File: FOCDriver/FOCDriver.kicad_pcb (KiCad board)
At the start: 4 copper layers, 80 x 80 mm, 306 parts, among them J1 Conn_02x06_Odd_Even, J10 Conn_01x04, J11 Conn_01x04, J12 Screw_Terminal_01x02, J2 Conn_02x06_Odd_Even, J3 Conn_02x06_Odd_Even, J4 Conn_02x05_Odd_Even, J5 Screw_Terminal_01x02, J6 Conn_01x03_Pin, J7 Conn_01x03_Pin, J8 Conn_01x03_Pin, J9 Conn_01x04, M1 Fan_Tacho_PWM, Q1 NMOS, Q2 SIR422DP-T1-GE3, SW1 SW_Push, SW2 SW_Push, SW3 SW_Push, U1 STM32H725IGTx, U10 DRV8316CR, U11 MCP1501-25xSN, U12 TMP1075DSG, U13 LM22676MR-5, U14 Si4435DDY, U15 DRV8316CR, U16 DRV8316CR, U17 ZXCT1109, U2 LM324, U3 24LC64, U4 LM324, U5 AP7375-30SA-7, U6 AMS1117-3.3, U7 LM324, Y1 Crystal_GND24

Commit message: Update
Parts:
- added C90: 100n, Footprints:Nice_0603C, F.Cu at (52.5, 97.5)
- added D8: APT2012SYCK, LED_SMD:LED_0805_2012Metric, F.Cu at (65.9, 101.4)
- added D9: APT2012SYCK, LED_SMD:LED_0805_2012Metric, F.Cu at (65.9, 103.3)
- added R80: DNP, Footprints:Nice_0402DNP, F.Cu at (52.8, 98.8)
- added R81: 1k, Footprints:Nice_0402R, F.Cu at (63.0, 101.5)
- added R82: 1k, Footprints:Nice_0402R, F.Cu at (63.6, 103.2)
- added kibuzzard-67FE68DD: G***, kibuzzard-67FE68DD, B.Cu at (52.3, 101.2)
- added kibuzzard-67FE6936: G***, kibuzzard-67FE6936, B.Cu at (52.2, 90.0)
- added kibuzzard-67FE6963: G***, kibuzzard-67FE6963, B.Cu at (52.2, 78.8)
- C43: footprint Capacitor_SMD:CP_Elec_10x10 -> Capacitor_SMD:CP_Elec_8x10.5
- C68, C69, C83: footprint Capacitor_SMD:CP_Elec_10x10 -> Capacitor_SMD:CP_Elec_10x10.5
- C92, C95, C96, C97: footprint Footprints:Nice_0805C -> Footprints:Nice_0603C
- D1: value 10V zener -> BZX384-B10,115
- D3, D4, D5, D6, D7: value LED -> APT2012SYCK
- F1: value 30R300U / 30R500U -> 30R500U
- L1: value L_Ferrite -> BLM18AG471SN1D
- Q1: value NMOS -> 2N7002
- R51, R52, R65: value 470 -> 470R
- R62, R69, R70, R74, R75: value 100 -> 100R
- RN1: value R_Pack04 -> EXB-38V102JV
- RN2, RN3, RN4, RN5: value R_Pack04 -> EXB-N8N220JX
- U11: value MCP1501-25xSN -> MCP1501-25E/SN
- Y1: value Crystal_GND24 -> ECS-250-18-33-JGN-TR3
- moved R2 10.5 mm to (51.5, 121.6), turned to 180 degrees
- moved D1 7.83 mm to (52.2, 120.1)
- moved R64 2.24 mm to (52.2, 101.2), turned to -90 degrees
- moved TP59 1.73 mm to (80.7, 90.4)
- moved TP4 1.06 mm to (62.2, 103.5)
- moved C43 0.82 mm to (57.5, 80.9)
- moved C69 0.58 mm to (78.7, 83.5)
- moved C68 0.50 mm to (100.0, 83.5)
- moved C83 0.40 mm to (121.6, 83.5)
- moved C97 0.30 mm to (111.3, 64.9)
- moved TP56 0.22 mm to (73.0, 107.3)
- moved J10 0.20 mm to (127.8, 91.1)
- moved R76 0.20 mm to (126.2, 95.1)
- moved R77 0.20 mm to (126.2, 97.1)
- moved kibuzzard-67FA3F2F 0.20 mm to (124.0, 90.6)
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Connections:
- net LED1 renamed /MCU/LED1
- net LED2 renamed /MCU/LED2
- net LED3 renamed /MCU/LED3
- net LED4 renamed /MCU/LED4
- U1 pad 50: /MCU/TIM2_CH1 -> unconnected-(U1-PA5-Pad50)
- U13 pad 2: unconnected-(U13-NC-Pad2) -> Net-(U13-SS)
- U13 pad 3: unconnected-(U13-NC-Pad3) -> Net-(U13-RT)
- U14 pad 1: Net-(J5-Pin_1) -> Net-(D1-K)
- U14 pad 2: Net-(J5-Pin_1) -> Net-(D1-K)
- U14 pad 3: Net-(J5-Pin_1) -> Net-(D1-K)
- U14 pad 5: Net-(D1-K) -> Net-(J5-Pin_1)
- U14 pad 6: Net-(D1-K) -> Net-(J5-Pin_1)
- U14 pad 7: Net-(D1-K) -> Net-(J5-Pin_1)
- U14 pad 8: Net-(D1-K) -> Net-(J5-Pin_1)
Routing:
- net +5V: track 68.7 -> 94.6 mm, vias 16 -> 23
- net GND: track 228.2 -> 243.9 mm, vias 328 -> 383
- net Net-(D1-K): track 0.00 -> 4.66 mm
- net MTR2_SDA: track 76.3 -> 80.0 mm
- net Net-(U2D-+): track 10.5 -> 7.24 mm
- net MTRx_SLEEP: track 104.8 -> 107.5 mm
- net /Motor1/NTC: track 48.3 -> 46.1 mm
- net EN_CLAMP: track 51.3 -> 53.3 mm
- net Net-(U13-SS): track 0.00 -> 1.86 mm
- net MTR3_SOA: track 30.5 -> 32.3 mm
- net MTR2_SCL: track 79.6 -> 81.4 mm
- net Net-(U13-RT): track 0.00 -> 1.75 mm
- net Net-(D9-A): track 0.00 -> 1.53 mm
- net Net-(D1-A): track 2.80 -> 4.31 mm
- net I2C4_SDA: track 9.32 -> 10.8 mm
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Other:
- board text added: "+3V3"
- board text added: "1"
- board text added: "2"
- board text added: "3"
- board text added: "4"
- board text added: "Im"
- board text added: "Vm"
- board text removed: "Imon"
- board text removed: "Vmotor"

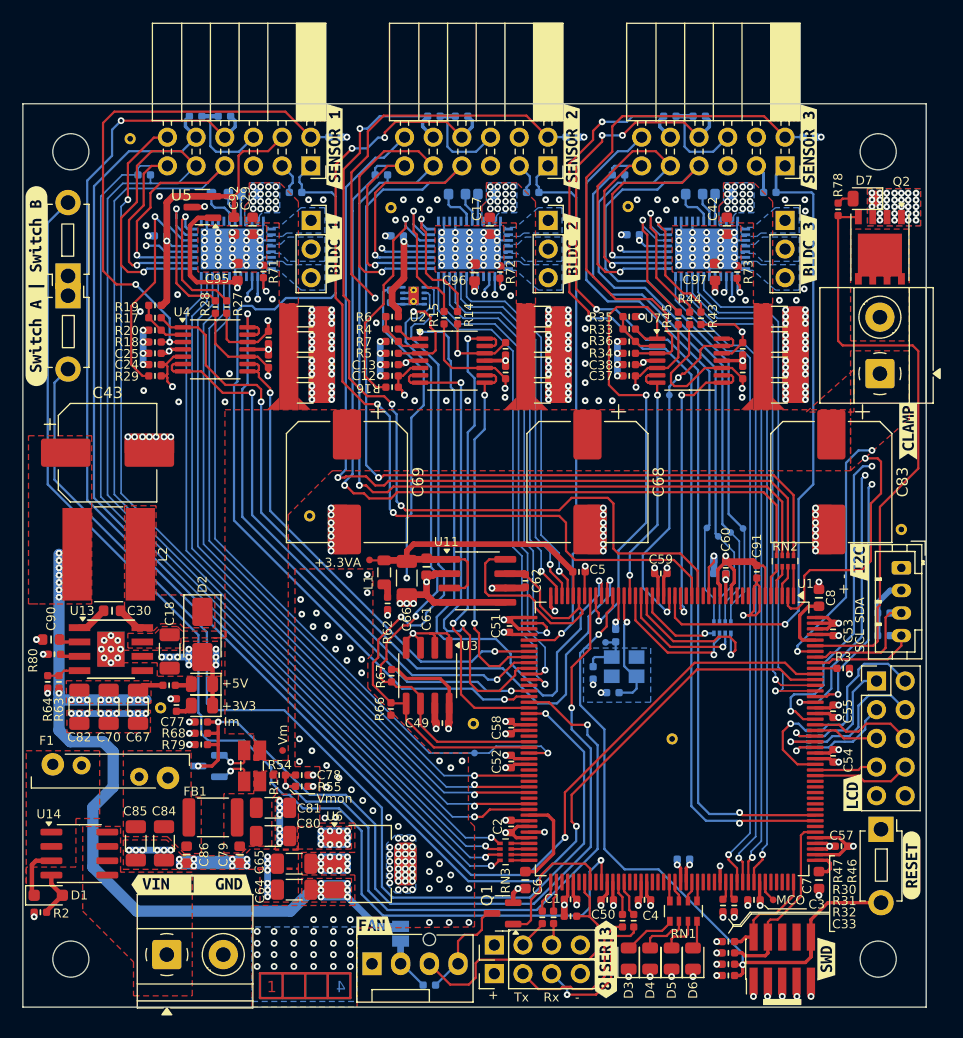
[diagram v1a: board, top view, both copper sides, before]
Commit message: Sensor PCB fixes labels
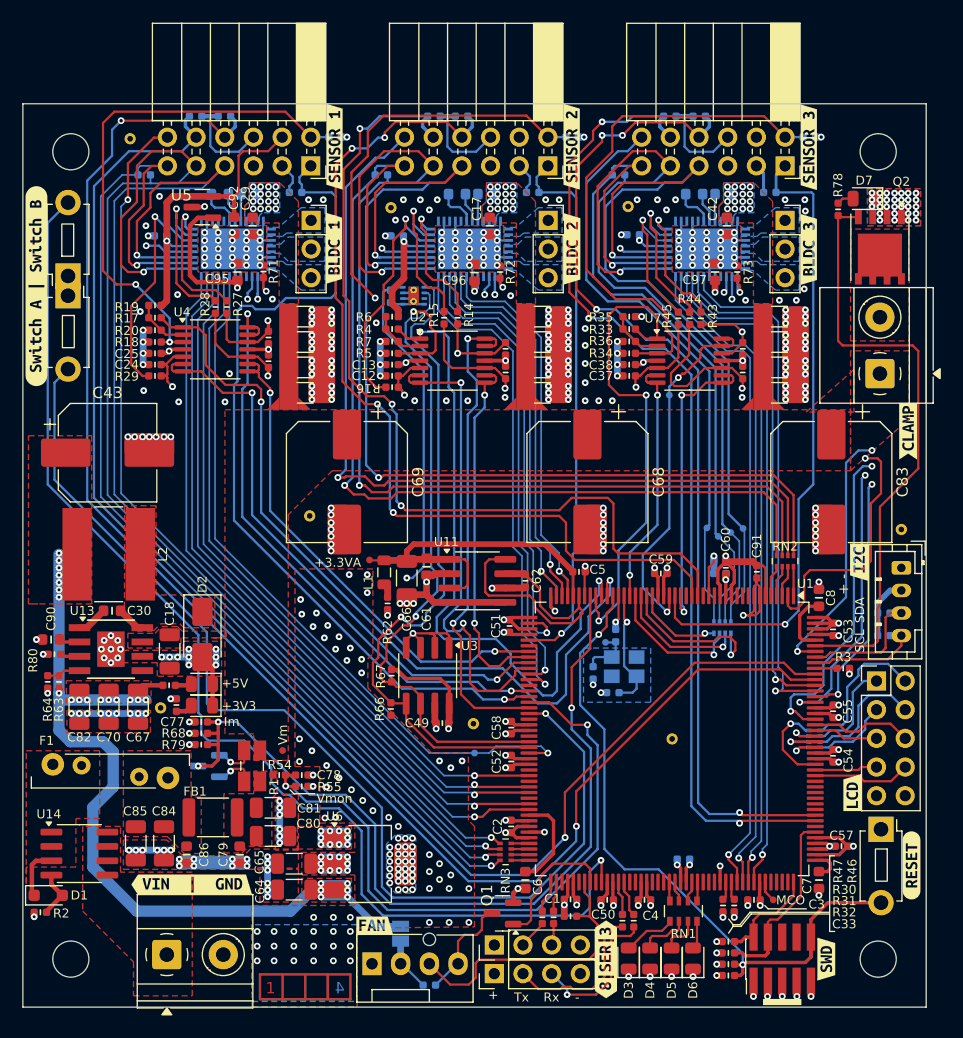
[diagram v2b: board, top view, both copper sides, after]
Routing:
- net VDD: track 127.6 -> 127.8 mm, vias 136 -> 130

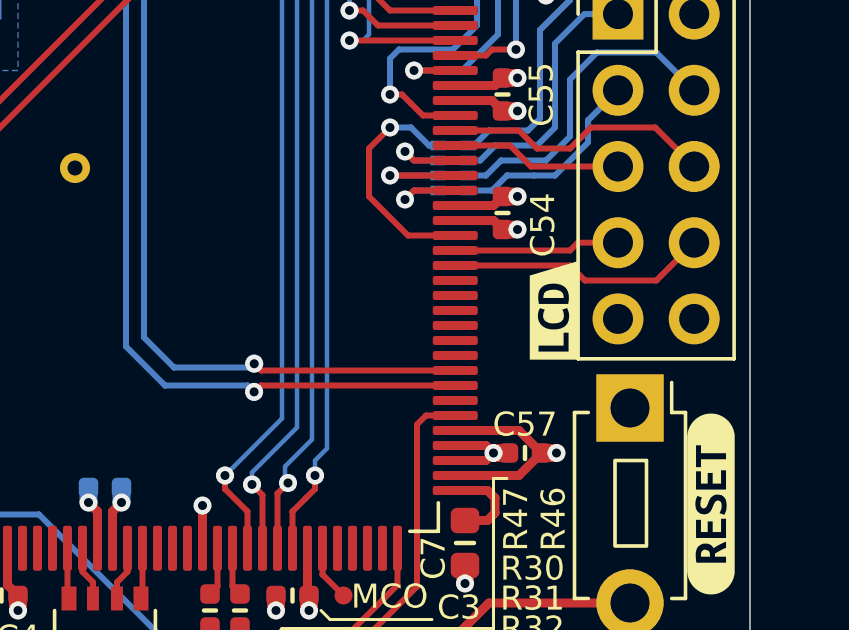
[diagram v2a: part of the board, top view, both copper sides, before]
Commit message: Untented vias for DRVOFF signal Added unallocated IOs for DRVOFF potentially
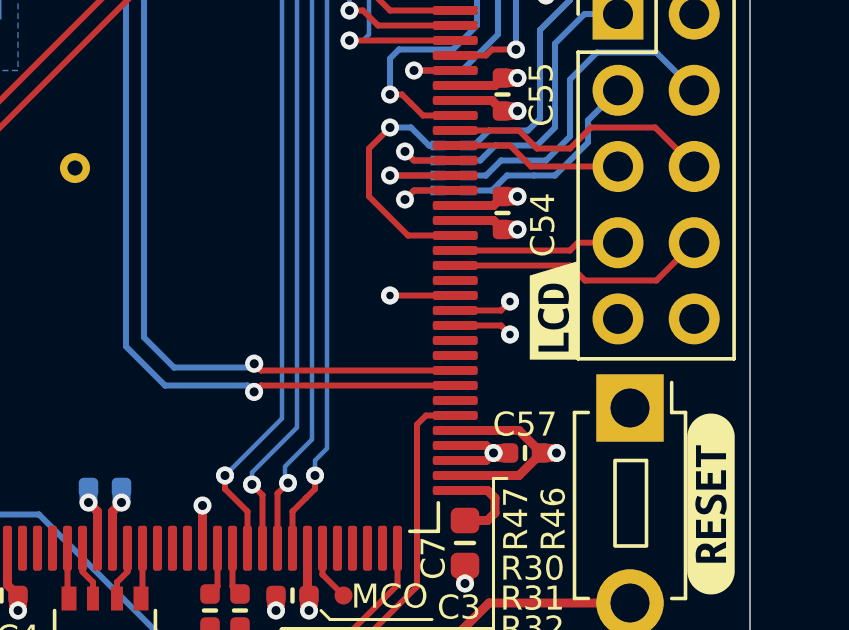
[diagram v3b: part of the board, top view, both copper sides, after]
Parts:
- added TP78: TestPoint, Footprints:TP_0.6mm, B.Cu at (122.0, 111.8)
- added TP79: TestPoint, Footprints:TP_0.6mm, B.Cu at (122.0, 110.7)
- added TP80: TestPoint, Footprints:TP_0.6mm, B.Cu at (118.0, 110.5)
- moved kibuzzard-67F3FF37 0.30 mm to (65.1, 122.5)
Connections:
- U1 pad 144: unconnected-(U1-PD1-Pad144) -> Net-(U1-PD1)
- U1 pad 145: unconnected-(U1-PD2-Pad145) -> Net-(U1-PD2)
- U1 pad 146: unconnected-(U1-PD3-Pad146) -> Net-(U1-PD3)
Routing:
- net Net-(U1-PD3): track 0.00 -> 2.17 mm, vias 0 -> 1
- net Net-(U1-PD2): track 0.00 -> 1.95 mm, vias 0 -> 1
- net Net-(U1-PD1): track 0.00 -> 1.95 mm, vias 0 -> 1
